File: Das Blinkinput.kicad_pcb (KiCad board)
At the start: 2 copper layers, 50.8 x 12.7 mm, 33 parts, among them P101 CONN_01X02, P102 CONN_01X01, P103 CONN_01X01, P104 CONN_01X01, P105 CONN_01X05, P201 CONN_01X01, P301 CONN_01X01, P401 CONN_01X01, P501 CONN_01X01, U101 LP2980IM5-3.0/NOPB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

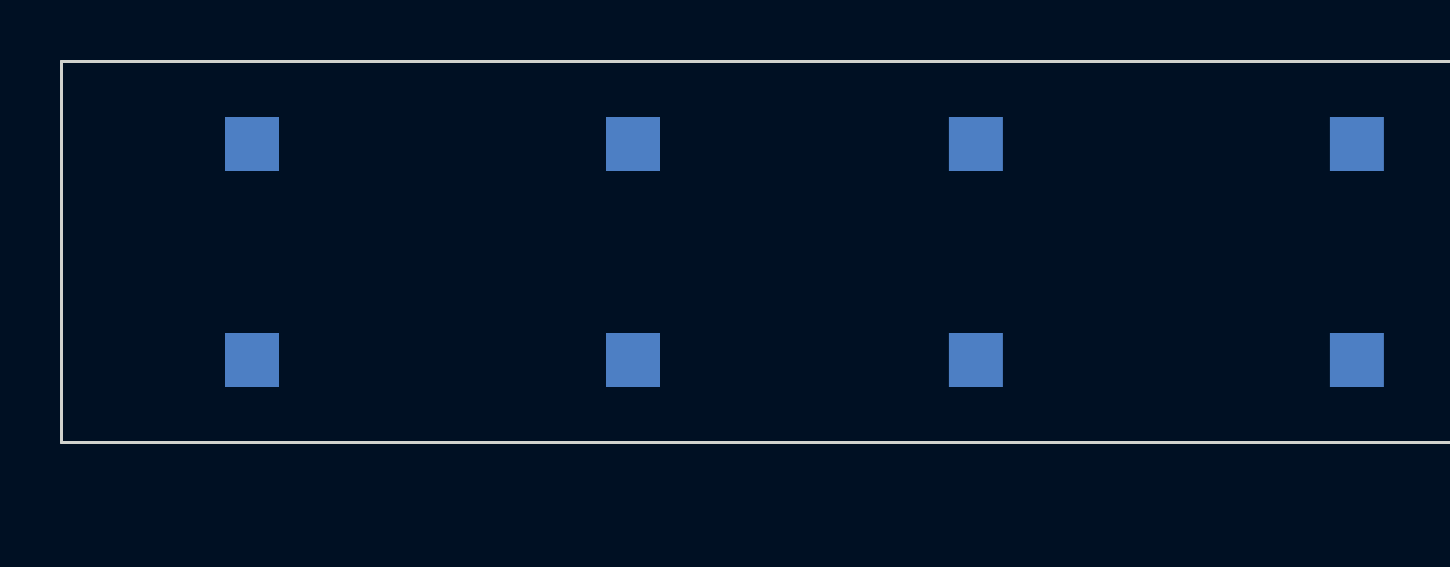
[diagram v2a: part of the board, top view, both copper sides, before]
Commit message: Added secondary footprint for photodiode
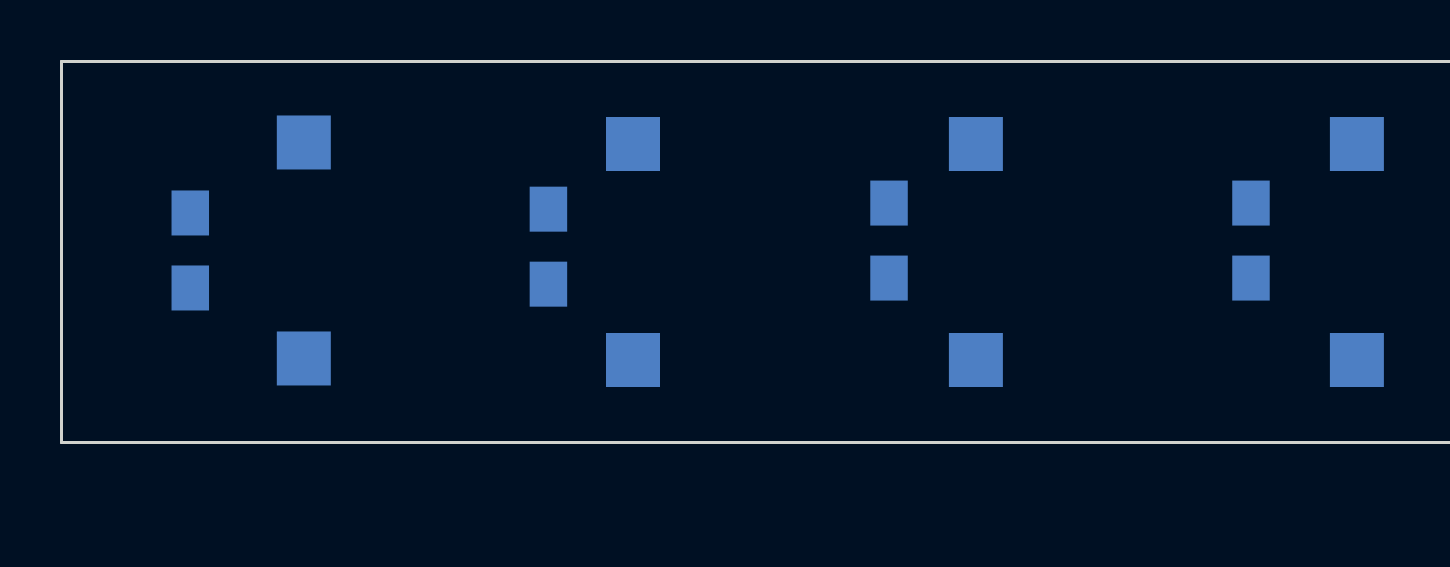
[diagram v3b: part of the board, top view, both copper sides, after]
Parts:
- added PD202: NOPOP, Capacitors_SMD:C_0805_HandSoldering, B.Cu at (81.8, 111.7)
- added PD302: NOPOP, Capacitors_SMD:C_0805_HandSoldering, B.Cu at (105.1, 111.4)
- added PD402: NOPOP, Capacitors_SMD:C_0805_HandSoldering, B.Cu at (117.1, 111.4)
- added PD502: NOPOP, Capacitors_SMD:C_0805_HandSoldering, B.Cu at (93.7, 111.6)
- moved PD201 1.73 mm to (85.5, 111.7)
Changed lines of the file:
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@@
 (kicad_pcb (version 4) (host pcbnew 0.201505141916+5653~23~ubuntu14.04.1-product)
   (general
-    (links 69)
-    (no_connects 69)
-    (area 76.099999 65.939999 199.858002 177.938001)
+    (links 77)
+    (no_connects 77)
+    (area 77.419999 105.359999 128.320001 118.160001)
     (thickness 1.6)
     (drawings 8)
     (tracks 0)
     (zones 0)
-    (modules 33)
+    (modules 37)
     (nets 21)
   )
@@
   )
   (module DasBlinkinput:VPW34SR (layer B.Cu)
-    (at 83.82 111.76 90)
+    (at 85.5472 111.7092 90)
     (fp_text reference PD201 (at 0 -3.5 90) (layer B.SilkS)
       (effects (font (size 1 1) (thickness 0.15)) (justify mirror))
@@
       (net 11 "Net-(C501-Pad2)"))
   )
+  (module Capacitors_SMD:C_0805_HandSoldering (layer B.Cu)
+    (at 81.7626 111.7092 90)
+    (descr "Capacitor SMD 0805, hand soldering")
+    (tags "capacitor 0805")
+    (attr smd)
+    (fp_text reference PD202 (at 0 2.1 90) (layer B.SilkS)
+      (effects (font (size 1 1) (thickness 0.15)) (justify mirror))
+    )
+    (fp_text value NOPOP (at 0 -2.1 90) (layer B.Fab)
+      (effects (font (size 1 1) (thickness 0.15)) (justify mirror))
+    )
+    (fp_line (start -2.3 1) (end 2.3 1) (layer B.CrtYd) (width 0.05))
+    (fp_line (start -2.3 -1) (end 2.3 -1) (layer B.CrtYd) (width 0.05))
+    (fp_line (start -2.3 1) (end -2.3 -1) (layer B.CrtYd) (width 0.05))
+    (fp_line (start 2.3 1) (end 2.3 -1) (layer B.CrtYd) (width 0.05))
+    (fp_line (start 0.5 0.85) (end -0.5 0.85) (layer B.SilkS) (width 0.15))
+    (fp_line (start -0.5 -0.85) (end 0.5 -0.85) (layer B.SilkS) (width 0.15))
+    (pad 1 smd rect (at -1.25 0 90) (size 1.5 1.25) (layers B.Cu B.Paste B.Mask)
+      (net 12 VGND))
+    (pad 2 smd rect (at 1.25 0 90) (size 1.5 1.25) (layers B.Cu B.Paste B.Mask)
+      (net 5 "Net-(C202-Pad2)"))
+    (model Capacitors_SMD.3dshapes/C_0805_HandSoldering.wrl
+      (at (xyz 0 0 0))
+      (scale (xyz 1 1 1))
+      (rotate (xyz 0 0 0))
+    )
+  )
+  (module Capacitors_SMD:C_0805_HandSoldering (layer B.Cu)
+    (at 105.0544 111.379 90)
+    (descr "Capacitor SMD 0805, hand soldering")
+    (tags "capacitor 0805")
+    (attr smd)
+    (fp_text reference PD302 (at 0 2.1 90) (layer B.SilkS)
+      (effects (font (size 1 1) (thickness 0.15)) (justify mirror))
+    )
+    (fp_text value NOPOP (at 0 -2.1 90) (layer B.Fab)
+      (effects (font (size 1 1) (thickness 0.15)) (justify mirror))
+    )
+    (fp_line (start -2.3 1) (end 2.3 1) (layer B.CrtYd) (width 0.05))
+    (fp_line (start -2.3 -1) (end 2.3 -1) (layer B.CrtYd) (width 0.05))
+    (fp_line (start -2.3 1) (end -2.3 -1) (layer B.CrtYd) (width 0.05))
+    (fp_line (start 2.3 1) (end 2.3 -1) (layer B.CrtYd) (width 0.05))
+    (fp_line (start 0.5 0.85) (end -0.5 0.85) (layer B.SilkS) (width 0.15))
+    (fp_line (start -0.5 -0.85) (end 0.5 -0.85) (layer B.SilkS) (width 0.15))
+    (pad 1 smd rect (at -1.25 0 90) (size 1.5 1.25) (layers B.Cu B.Paste B.Mask)
+      (net 12 VGND))
+    (pad 2 smd rect (at 1.25 0 90) (size 1.5 1.25) (layers B.Cu B.Paste B.Mask)
+      (net 7 "Net-(C301-Pad2)"))
+    (model Capacitors_SMD.3dshapes/C_0805_HandSoldering.wrl
+      (at (xyz 0 0 0))
+      (scale (xyz 1 1 1))
+      (rotate (xyz 0 0 0))
+    )
+  )
+  (module Capacitors_SMD:C_0805_HandSoldering (layer B.Cu)
+    (at 117.1194 111.379 90)
+    (descr "Capacitor SMD 0805, hand soldering")
+    (tags "capacitor 0805")
+    (attr smd)
+    (fp_text reference PD402 (at 0 2.1 90) (layer B.SilkS)
+      (effects (font (size 1 1) (thickness 0.15)) (justify mirror))
+    )
+    (fp_text value NOPOP (at 0 -2.1 90) (layer B.Fab)
+      (effects (font (size 1 1) (thickness 0.15)) (justify mirror))
+    )
+    (fp_line (start -2.3 1) (end 2.3 1) (layer B.CrtYd) (width 0.05))
+    (fp_line (start -2.3 -1) (end 2.3 -1) (layer B.CrtYd) (width 0.05))
+    (fp_line (start -2.3 1) (end -2.3 -1) (layer B.CrtYd) (width 0.05))
+    (fp_line (start 2.3 1) (end 2.3 -1) (layer B.CrtYd) (width 0.05))
+    (fp_line (start 0.5 0.85) (end -0.5 0.85) (layer B.SilkS) (width 0.15))
+    (fp_line (start -0.5 -0.85) (end 0.5 -0.85) (layer B.SilkS) (width 0.15))
+    (pad 1 smd rect (at -1.25 0 90) (size 1.5 1.25) (layers B.Cu B.Paste B.Mask)
+      (net 12 VGND))
+    (pad 2 smd rect (at 1.25 0 90) (size 1.5 1.25) (layers B.Cu B.Paste B.Mask)
+      (net 9 "Net-(C401-Pad2)"))
+    (model Capacitors_SMD.3dshapes/C_0805_HandSoldering.wrl
+      (at (xyz 0 0 0))
+      (scale (xyz 1 1 1))
+      (rotate (xyz 0 0 0))
+    )
+  )
+  (module Capacitors_SMD:C_0805_HandSoldering (layer B.Cu)
+    (at 93.7006 111.5822 90)
+    (descr "Capacitor SMD 0805, hand soldering")
+    (tags "capacitor 0805")
+    (attr smd)
+    (fp_text reference PD502 (at 0 2.1 90) (layer B.SilkS)
+      (effects (font (size 1 1) (thickness 0.15)) (justify mirror))
+    )
+    (fp_text value NOPOP (at 0 -2.1 90) (layer B.Fab)
+      (effects (font (size 1 1) (thickness 0.15)) (justify mirror))
+    )
+    (fp_line (start -2.3 1) (end 2.3 1) (layer B.CrtYd) (width 0.05))
+    (fp_line (start -2.3 -1) (end 2.3 -1) (layer B.CrtYd) (width 0.05))
+    (fp_line (start -2.3 1) (end -2.3 -1) (layer B.CrtYd) (width 0.05))
+    (fp_line (start 2.3 1) (end 2.3 -1) (layer B.CrtYd) (width 0.05))
+    (fp_line (start 0.5 0.85) (end -0.5 0.85) (layer B.SilkS) (width 0.15))
+    (fp_line (start -0.5 -0.85) (end 0.5 -0.85) (layer B.SilkS) (width 0.15))
+    (pad 1 smd rect (at -1.25 0 90) (size 1.5 1.25) (layers B.Cu B.Paste B.Mask)
+      (net 12 VGND))
+    (pad 2 smd rect (at 1.25 0 90) (size 1.5 1.25) (layers B.Cu B.Paste B.Mask)
+      (net 11 "Net-(C501-Pad2)"))
+    (model Capacitors_SMD.3dshapes/C_0805_HandSoldering.wrl
+      (at (xyz 0 0 0))
+      (scale (xyz 1 1 1))
+      (rotate (xyz 0 0 0))
+    )
+  )
   (gr_line (start 77.47 105.41) (end 77.47 118.11) (angle 90) (layer Edge.Cuts) (width 0.1))
